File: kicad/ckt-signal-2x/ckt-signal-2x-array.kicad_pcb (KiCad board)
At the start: 2 copper layers, 81.9 x 221.2 mm, 226 parts, among them J1 Screw_Terminal_01x08

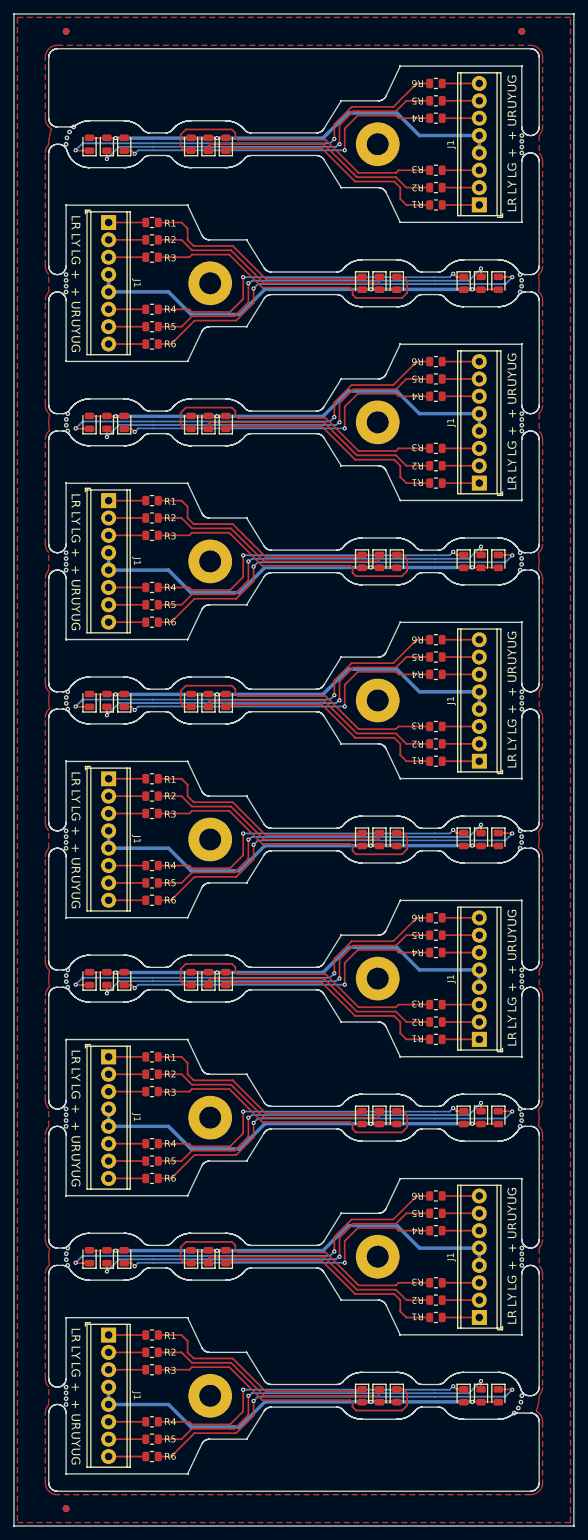
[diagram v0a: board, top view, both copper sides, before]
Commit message: Fixed Nathan's dangling traces
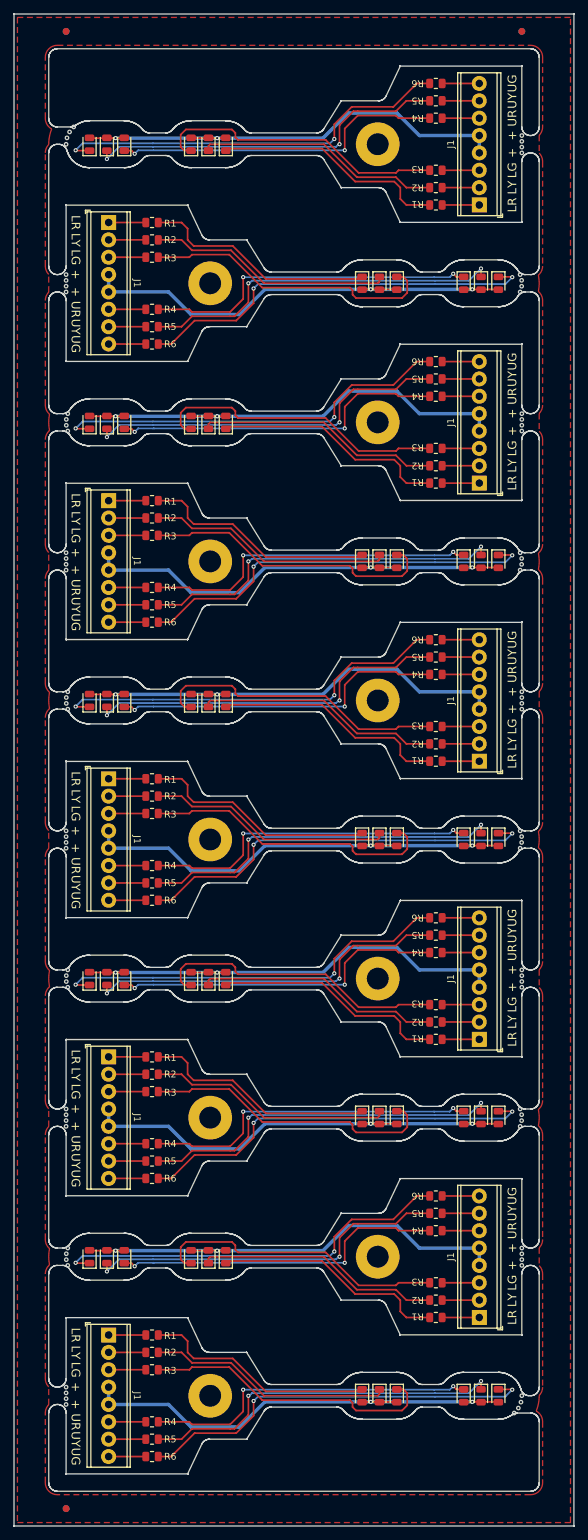
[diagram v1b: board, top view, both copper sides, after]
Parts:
- removed the D3 at (133.5, 201.8)
- removed the D5 at (121.1, 201.8)
- removed the H1 at (136.2, 100.1)
- removed the R1 at (169.3, 210.7)
- removed the R5 at (169.3, 195.5)
- added D1: RED, LED_SMD:LED_0805_2012Metric, F.Cu at (138.5, 201.8)
- added D2: AMBER, LED_SMD:LED_0805_2012Metric, F.Cu at (136.0, 201.8)
- added D4: RED, LED_SMD:LED_0805_2012Metric, F.Cu at (123.7, 201.8)
- added R2: 1k, Resistor_SMD:R_0805_2012Metric, F.Cu at (169.3, 208.2)
- added R3: 1k, Resistor_SMD:R_0805_2012Metric, F.Cu at (169.3, 205.6)
- D3: renamed from D4; value RED -> GREEN
- D6: renamed from D1; value RED -> GREEN
- H1: renamed from D6; value GREEN -> MountingHole; footprint LED_SMD:LED_0805_2012Metric -> MountingHole:MountingHole_3.2mm_M3_Pad
- moved D6 118.0 mm to (178.4, 100.1), turned to -90 degrees
- moved H1 42.2 mm to (136.2, 100.1)
- moved D6 19.9 mm to (118.6, 201.8)
- moved D5 14.9 mm to (121.1, 201.8)
- moved R5 10.2 mm to (169.3, 195.5)
- moved D3 9.78 mm to (133.5, 201.8)
- moved R1 2.54 mm to (169.3, 210.7)
- renumbered D2 to D5, R2 to R1, R3 to R5
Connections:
- D3 pad 1: Board_8-Net-(D4-Pad1) -> Board_8-Net-(D3-Pad1)
- D5 pad 1: Board_8-Net-(D2-Pad1) -> Board_8-Net-(D5-Pad1)
- D6 pad 1: Board_8-Net-(D6-Pad1) -> Board_3-Net-(D6-Pad1)
- D6 pad 2: Board_8-Net-(D1-Pad2) -> Board_3-Net-(D1-Pad2)
- D6 pad 1: Board_8-Net-(D1-Pad1) -> Board_8-Net-(D6-Pad1)
- H1 pad 1: Board_3-Net-(D6-Pad1) -> Board_3-unconnected-(H1-Pad1)
- R1 pad 1: Board_8-Net-(D2-Pad1) -> Board_8-Net-(D1-Pad1)
- R1 pad 2: Board_8-Net-(R2-Pad2) -> Board_8-Net-(R1-Pad2)
- R5 pad 1: Board_8-Net-(D3-Pad1) -> Board_8-Net-(D5-Pad1)
- R5 pad 2: Board_8-Net-(R3-Pad2) -> Board_8-Net-(J1-Pad7)
